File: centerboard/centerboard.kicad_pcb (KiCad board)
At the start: 2 copper layers, 66 parts, among them J1 Conn_01x10_MountingPin, J2 Conn_01x10_MountingPin, J3 Conn_01x10_MountingPin, J4 Conn_01x10_MountingPin, J5 Conn_01x10_MountingPin, J6 Conn_01x10_MountingPin, J7 Conn_01x10_MountingPin, J8 Conn_01x10_MountingPin, J9 Conn_01x10_MountingPin, U1 ProMicro

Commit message: redo centerboard again (and again)
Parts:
- added REF**: MountingHole_3.2mm_M3, MountingHole:MountingHole_3.2mm_M3, F.Cu at (206.5, 53.0)
- added REF**: MountingHole_3.2mm_M3, MountingHole:MountingHole_3.2mm_M3, F.Cu at (181.5, 53.0)
- added REF**: SolderWirePad_1x01_SMD_1x2mm, Connector_Wire:SolderWirePad_1x01_SMD_1x2mm, F.Cu at (189.0, 57.5)
- added REF**: MountingHole_3.2mm_M3, MountingHole:MountingHole_3.2mm_M3, F.Cu at (205.0, 85.0)
- added REF**: MountingHole_3.2mm_M3, MountingHole:MountingHole_3.2mm_M3, F.Cu at (183.0, 85.0)
- moved D52 155.1 mm to (213.4, 81.5)
- moved D54 154.4 mm to (213.6, 79.5)
- moved D51 152.3 mm to (210.1, 82.5)
- moved D53 151.3 mm to (210.1, 80.5)
- moved J5 132.5 mm to (219.4, 62.8), turned to 90 degrees
- moved D34 130.6 mm to (213.6, 69.0), turned to 0 degrees
- moved J4 128.6 mm to (226.4, 55.2), turned to 90 degrees
- moved D36 127.9 mm to (213.6, 67.0), turned to 0 degrees
- moved D33 127.9 mm to (210.1, 70.0), turned to 0 degrees
- moved J8 126.5 mm to (219.4, 77.5), turned to 90 degrees
- moved J9 126.3 mm to (194.0, 85.5)
- moved D35 125.2 mm to (210.1, 68.0), turned to 0 degrees
- moved D38 125.1 mm to (213.5, 64.5), turned to 0 degrees
- moved D26 122.9 mm to (213.6, 60.5), turned to 0 degrees
- moved D40 122.5 mm to (213.6, 62.5), turned to 0 degrees
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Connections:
- U1 pad 1: SGDX -> ROW_1
- U1 pad 10: ROW_4 -> ROW_8
- U1 pad 11: COL_R3 -> COL_T
- U1 pad 12: COL_L2 -> SGDY
- U1 pad 13: COL_R1 -> SGDX
- U1 pad 14: COL_T -> COL_R3
- U1 pad 15: ROW_8 -> SGCLK
- U1 pad 16: ROW_7 -> ROW_5
- U1 pad 18: ROW_5 -> ROW_2
- U1 pad 19: COL_L1 -> COL_R2
- U1 pad 2: SGCLK -> COL_L1
- U1 pad 20: COL_R2 -> COL_R1
- U1 pad 5: SGDY -> ROW_3
- U1 pad 6: COL_L3 -> COL_L2
- U1 pad 7: ROW_1 -> ROW_7
- U1 pad 8: ROW_2 -> COL_L3
- U1 pad 9: ROW_3 -> ROW_4
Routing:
- net ROW_1: track 10.4 -> 123.7 mm, vias 1 -> 7
- net ROW_2: track 2.56 -> 114.7 mm, vias 1 -> 8
- net ROW_8: track 1.06 -> 106.8 mm, vias 1 -> 6
- net ROW_6: track 2.56 -> 106.8 mm, vias 1 -> 8
- net ROW_4: track 1.06 -> 102.8 mm, vias 1 -> 7
- net ROW_3: track 7.21 -> 104.0 mm, vias 6 -> 7
- net ROW_5: track 16.2 -> 106.4 mm, vias 6 -> 7
- net ROW_7: track 24.5 -> 104.9 mm, vias 6 -> 7
- net COL_T: track 0.00 -> 67.8 mm
- net GND: track 0.00 -> 33.9 mm, vias 0 -> 1
- net COL_R3: track 2.31 -> 32.5 mm, vias 1 -> 0
- net VCC: track 0.00 -> 29.0 mm, vias 0 -> 1
- net COL_L3: track 2.31 -> 31.0 mm, vias 1 -> 0
- net COL_R1: track 2.31 -> 30.7 mm, vias 1 -> 0
- net COL_L1: track 2.31 -> 30.5 mm, vias 1 -> 0
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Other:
- board outline added: 71 x 38.2 mm
- board text added: "GULL v1"

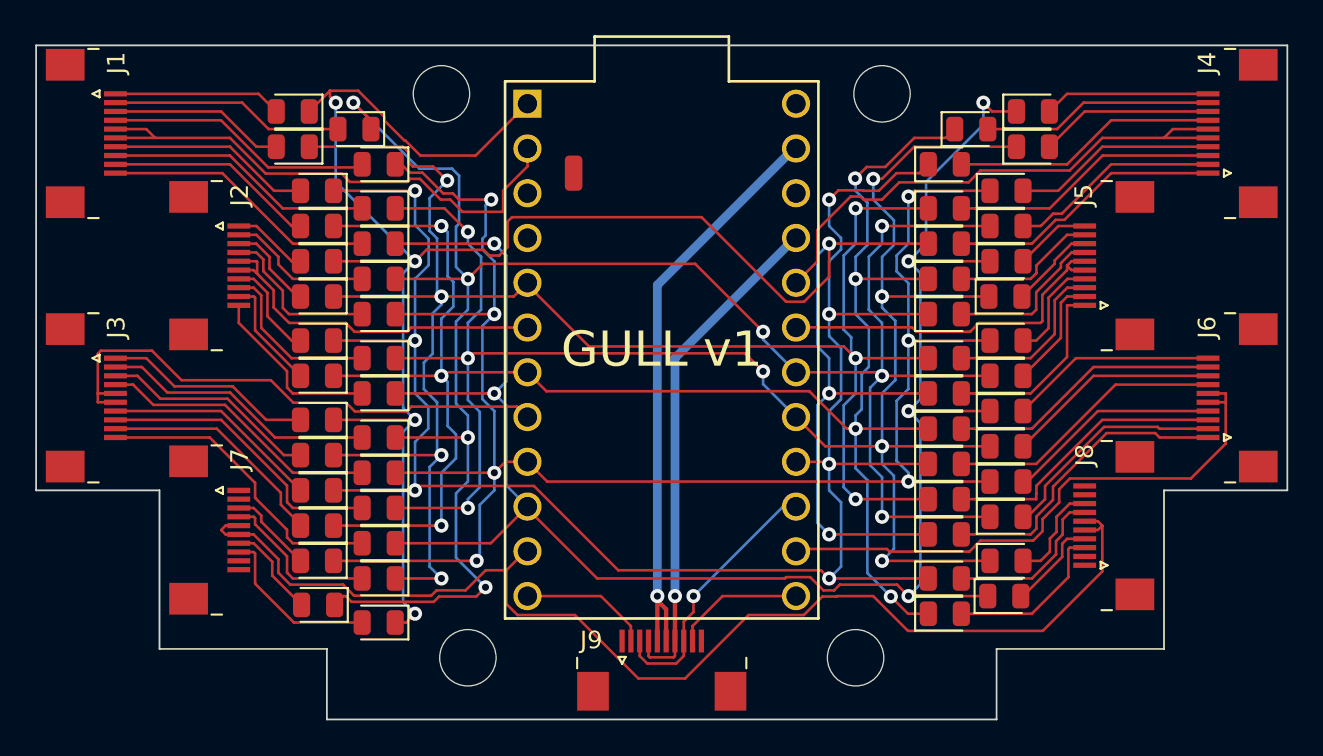
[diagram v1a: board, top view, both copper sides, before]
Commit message: Rework centerboard yet again. Now with vertical FFC headers and a ground pour.
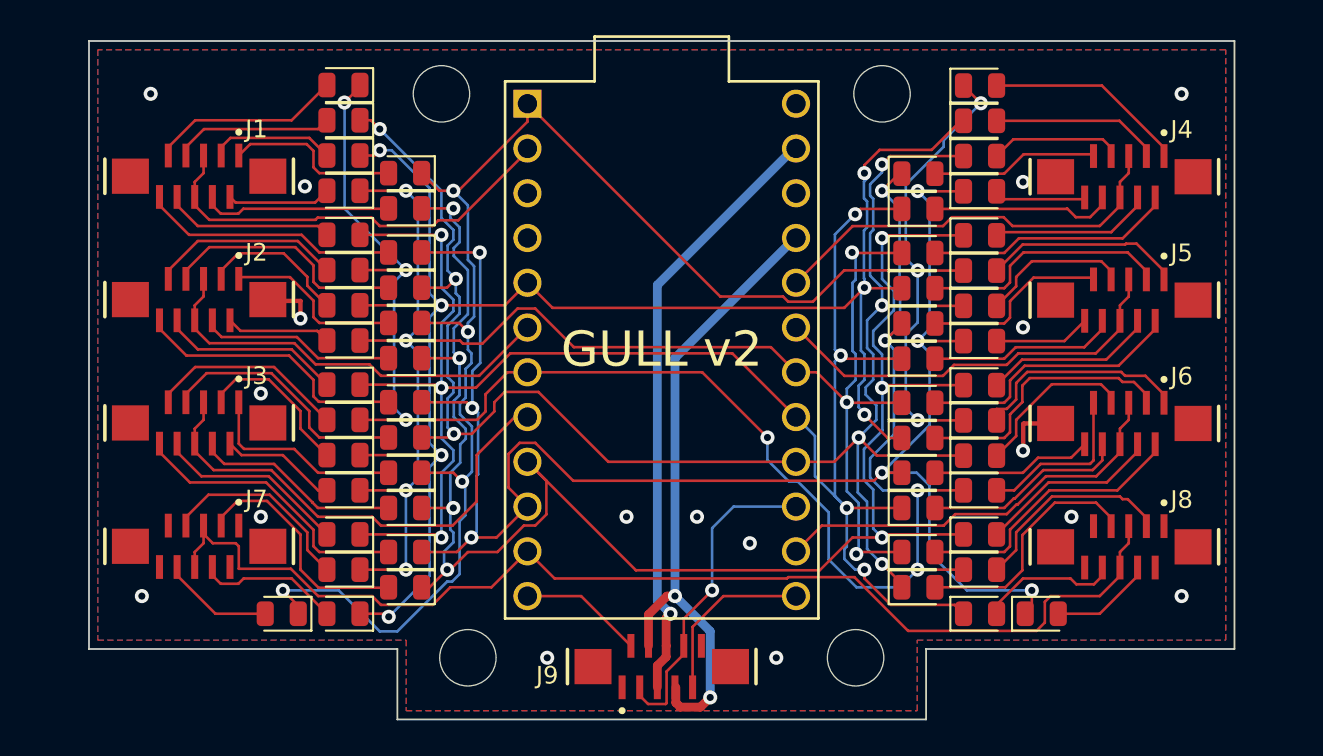
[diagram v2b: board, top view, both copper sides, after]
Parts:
- removed the REF** at (189.0, 57.5)
- J1, J2, J3, J4, J5, J6, J7, J8, J9: footprint Custom:FFC_Clamshell_0.5mm_1x10 -> Custom:GCT_FFC2A33-10-T-R_REVA_MPs
- moved D25 9.19 mm to (212.1, 52.5)
- moved D7 8.14 mm to (175.9, 52.5)
- moved D30 7.40 mm to (208.6, 59.5)
- moved D1 7.27 mm to (179.4, 57.5)
- moved D33 7.25 mm to (212.1, 63.0)
- moved D41 6.77 mm to (212.1, 71.5)
- moved J4 6.67 mm to (220.2, 57.7), turned to 180 degrees
- moved J1 6.66 mm to (167.8, 57.7), turned to 180 degrees
- moved J6 6.37 mm to (220.2, 71.7), turned to 180 degrees
- moved J3 6.36 mm to (167.8, 71.7), turned to 180 degrees
- moved D15 6.18 mm to (175.9, 63.0)
- moved D23 6.18 mm to (175.9, 71.5)
- moved D9 6.10 mm to (179.4, 66.0)
- moved D46 6.10 mm to (208.6, 76.5)
- moved D48 6.10 mm to (208.6, 74.5)
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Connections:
- J1 pad MP: unconnected-(J1-MountPin-PadMP) -> GND
- J2 pad MP: unconnected-(J2-MountPin-PadMP) -> GND
- J3 pad MP: unconnected-(J3-MountPin-PadMP) -> GND
- J4 pad MP: unconnected-(J4-MountPin-PadMP) -> GND
- J5 pad MP: unconnected-(J5-MountPin-PadMP) -> GND
- J6 pad MP: unconnected-(J6-MountPin-PadMP) -> GND
- J7 pad MP: unconnected-(J7-MountPin-PadMP) -> GND
- J8 pad MP: unconnected-(J8-MountPin-PadMP) -> GND
- J9 pad MP: unconnected-(J9-MountPin-PadMP) -> GND
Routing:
- net ROW_2: track 114.7 -> 87.7 mm, vias 8 -> 7
- net ROW_1: track 123.7 -> 106.2 mm
- net ROW_8: track 106.8 -> 94.8 mm, vias 6 -> 7
- net ROW_5: track 106.4 -> 94.7 mm
- net ROW_3: track 104.0 -> 94.2 mm
- net COL_R3: track 32.5 -> 23.3 mm
- net Net-(D18-A): track 15.7 -> 6.60 mm
- net Net-(D34-A): track 6.53 -> 14.8 mm
- net Net-(D29-A): track 15.0 -> 7.09 mm
- net Net-(D13-A): track 5.73 -> 13.6 mm
- net Net-(D59-A): track 4.94 -> 12.6 mm
- net VCC: track 29.0 -> 36.6 mm, vias 1 -> 2
- net COL_R1: track 30.7 -> 23.2 mm
- net Net-(D2-A): track 13.2 -> 5.91 mm
- net ROW_6: track 106.8 -> 99.5 mm, vias 8 -> 7
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- added copper zone on B.Cu, net GND
- added copper zone on F.Cu, net GND
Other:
- board size 71 x 38.2 mm -> 65 x 38.5 mm
- board text added: "GULL v2"
- board text removed: "GULL v1"

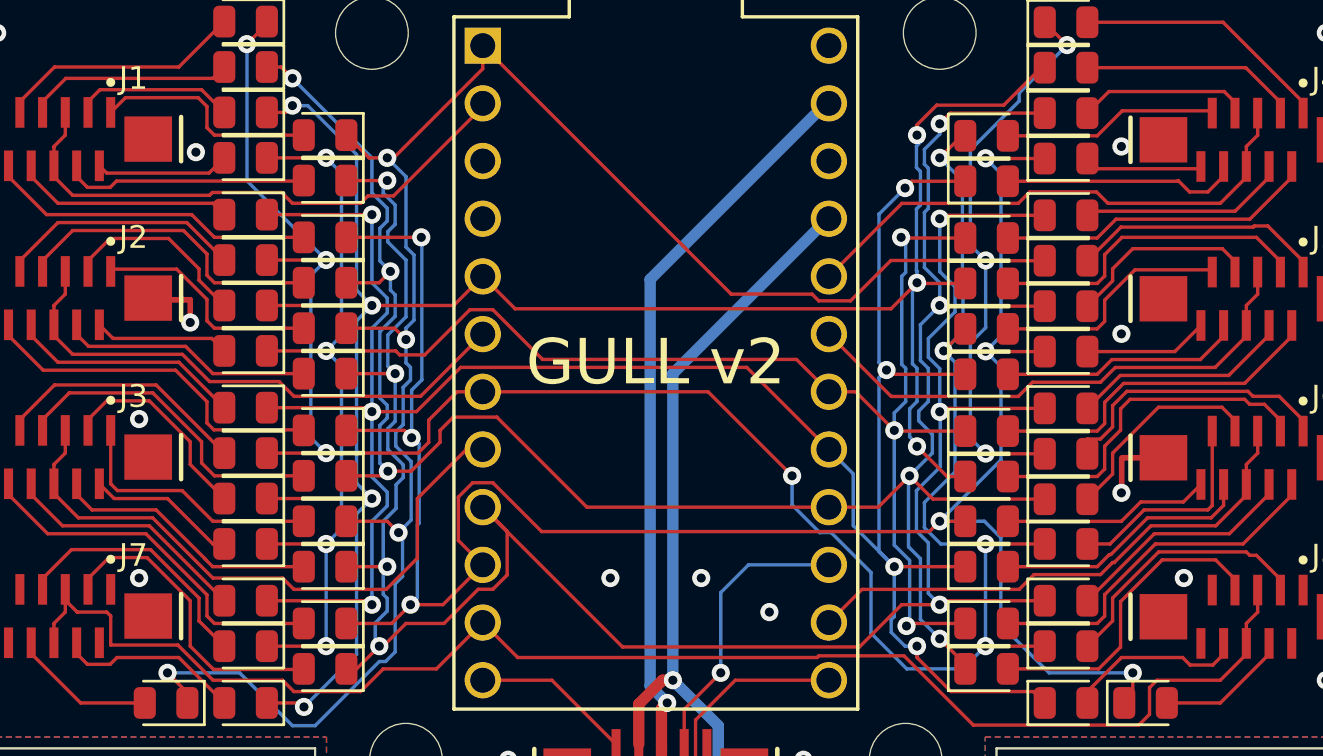
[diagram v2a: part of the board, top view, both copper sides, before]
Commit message: Add some redundant traces to centerboard to fix benign DRC violations
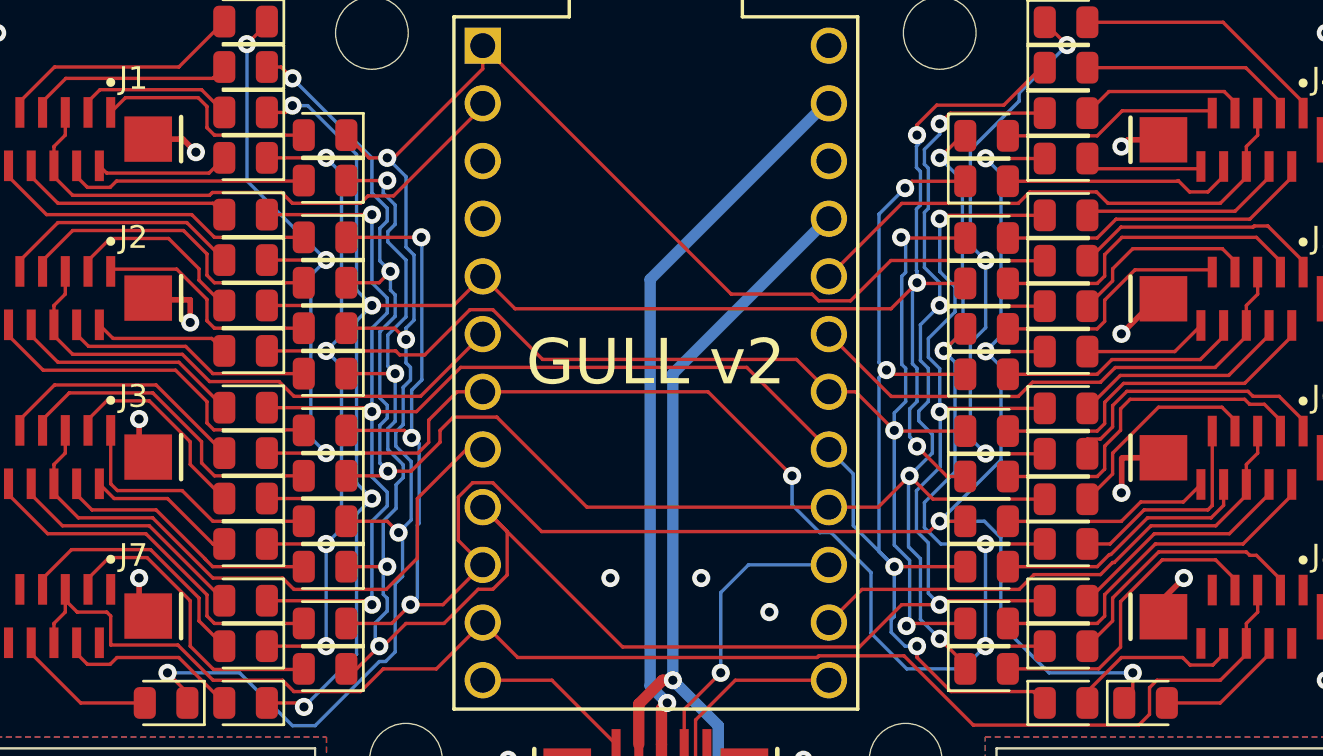
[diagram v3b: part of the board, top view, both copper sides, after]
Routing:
- net GND: track 40.7 -> 53.2 mm
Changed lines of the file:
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@@
   (segment (start 194.75 81.5) (end 194.75 68) (width 0.5) (layer "B.Cu") (net 87))
   (segment (start 194.75 68) (end 201.57 61.18) (width 0.5) (layer "B.Cu") (net 87))
+  (segment (start 216.35 64.705) (end 216.045 64.705) (width 0.25) (layer "F.Cu") (net 88))
+  (segment (start 216.045 64.705) (end 214.5 66.25) (width 0.25) (layer "F.Cu") (net 88))
+  (segment (start 173.175 57.675) (end 173.75 58.25) (width 0.25) (layer "F.Cu") (net 88))
+  (segment (start 214.795 57.705) (end 214.5 58) (width 0.25) (layer "F.Cu") (net 88))
+  (segment (start 171.25 71.275) (end 171.65 71.675) (width 0.25) (layer "F.Cu") (net 88))
   (segment (start 171.725 64.75) (end 171.65 64.675) (width 0.25) (layer "F.Cu") (net 88))
   (segment (start 193.75 85.45) (end 193.75 86.675) (width 0.5) (layer "F.Cu") (net 88))
+  (segment (start 216.35 57.705) (end 214.795 57.705) (width 0.25) (layer "F.Cu") (net 88))
+  (segment (start 171.25 70) (end 171.25 71.275) (width 0.25) (layer "F.Cu") (net 88))
   (segment (start 194.25 84.325) (end 194.25 84.95) (width 0.5) (layer "F.Cu") (net 88))
   (segment (start 214.5125 71.7375) (end 214.545 71.705) (width 0.25) (layer "F.Cu") (net 88))
+  (segment (start 171.25 77) (end 171.25 78.275) (width 0.25) (layer "F.Cu") (net 88))
   (segment (start 214.545 71.705) (end 216.35 71.705) (width 0.25) (layer "F.Cu") (net 88))
+  (segment (start 216.35 77.9) (end 217.25 77) (width 0.25) (layer "F.Cu") (net 88))
   (segment (start 194.25 84.95) (end 193.75 85.45) (width 0.5) (layer "F.Cu") (net 88))
   (segment (start 173.5 64.75) (end 171.725 64.75) (width 0.25) (layer "F.Cu") (net 88))
+  (segment (start 171.65 57.675) (end 173.175 57.675) (width 0.25) (layer "F.Cu") (net 88))
+  (segment (start 171.25 78.275) (end 171.65 78.675) (width 0.25) (layer "F.Cu") (net 88))
   (segment (start 173.5 64.75) (end 173.5 65.75) (width 0.25) (layer "F.Cu") (net 88))
+  (segment (start 216.35 78.705) (end 216.35 77.9) (width 0.25) (layer "F.Cu") (net 88))
   (segment (start 214.5125 73.2375) (end 214.5125 71.7375) (width 0.25) (layer "F.Cu") (net 88))
   (segment (start 214.5 73.25) (end 214.5125 73.2375) (width 0.25) (layer "F.Cu") (net 88))
